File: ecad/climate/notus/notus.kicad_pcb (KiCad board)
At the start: 2 copper layers, 115 x 23 mm, 7 parts, among them J1 640454-2

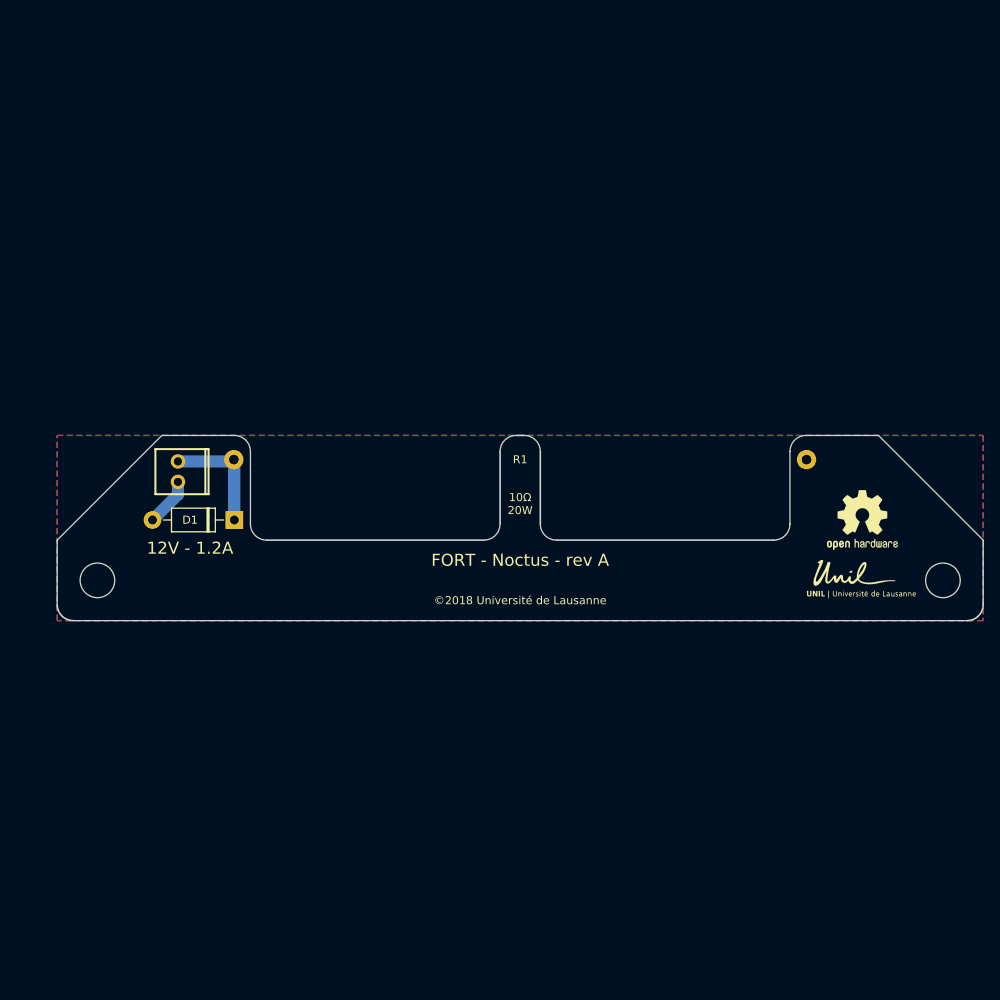
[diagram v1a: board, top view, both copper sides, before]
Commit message: Updates ecad for assembly production
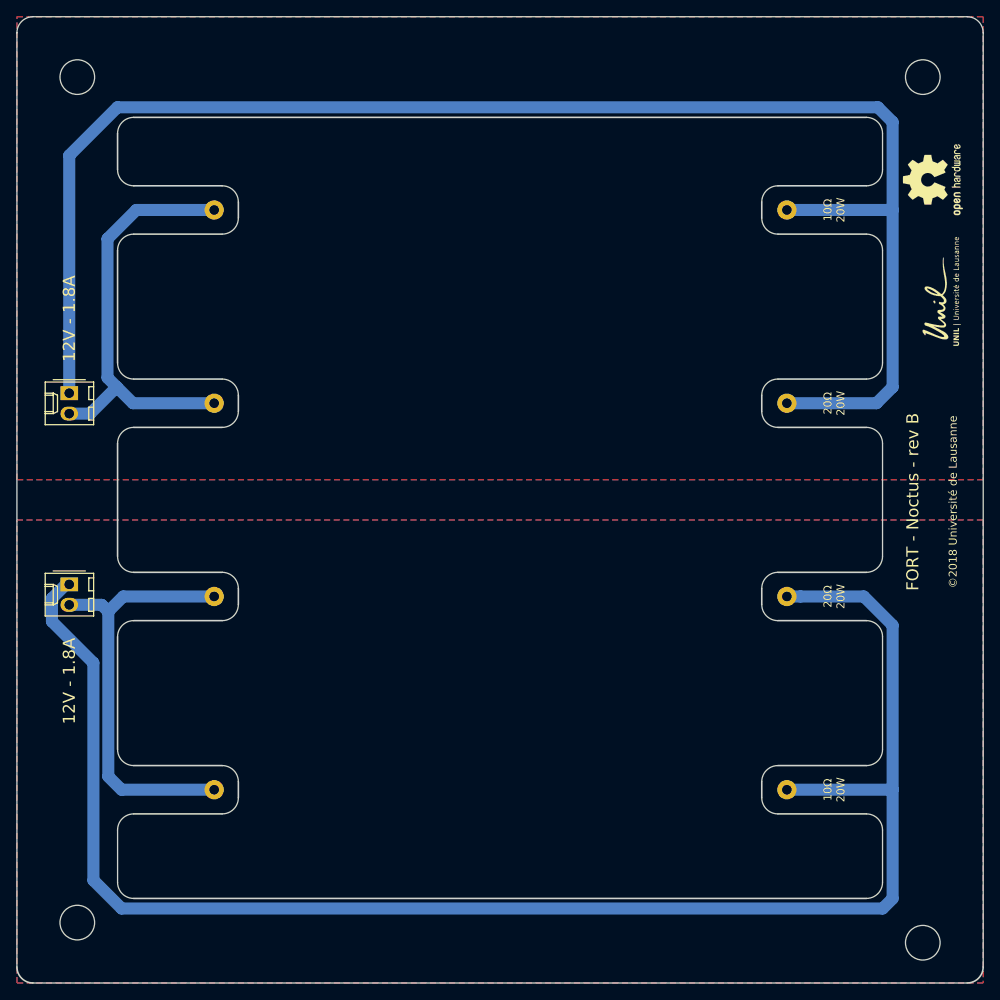
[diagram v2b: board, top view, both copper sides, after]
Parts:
- removed D1: 1N4001, Diode_THT:D_DO-41_SOD81_P10.16mm_Horizontal
- added J2: 6410-02A, Connector_Molex:Molex_KK-254_AE-6410-02A_1x02_P2.54mm_Vertical, F.Cu at (96.5, 76.8)
- added MH3: MountingHole, MountingHole:MountingHole_4.3mm_M4_DIN965, F.Cu at (202.5, 37.5)
- added MH4: MountingHole, MountingHole:MountingHole_4.3mm_M4_DIN965, F.Cu at (97.5, 37.5)
- added R2: 20R, 20W, Resistor_THT:R_Axial_Power_L60.0mm_W14.0mm_P71.12mm, F.Cu at (114.5, 102.0)
- added R3: 20R, 20W, Resistor_THT:R_Axial_Power_L60.0mm_W14.0mm_P71.12mm, F.Cu at (114.5, 54.0)
- added R4: 10R, 20W, Resistor_THT:R_Axial_Power_L60.0mm_W14.0mm_P71.12mm, F.Cu at (114.5, 78.0)
- J1: value 640454-2 -> 6410-02A; footprint FORT:640454-2 -> Connector_Molex:Molex_KK-254_AE-6410-02A_1x02_P2.54mm_Vertical
- moved R1 55.9 mm to (114.5, 126.0), turned to 0 degrees
- moved MH2 45.1 mm to (202.5, 145.0)
- moved REF** 43.1 mm to (203.8, 50.2), turned to 90 degrees
- moved MH1 42.6 mm to (97.5, 142.5)
- moved G*** 37.4 mm to (205.0, 64.0), turned to 90 degrees
- moved J1 19.4 mm to (96.5, 100.5)
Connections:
- net /PWM_+ renamed /PWM_A
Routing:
- net /PWM_B: track 0.00 -> 195.0 mm
- net /PWM_A: track 14.6 -> 202.9 mm
- net GNDA: track 0.00 -> 53.8 mm
- net GND: track 6.04 -> 53.4 mm
- added copper zone on B.Cu, net GNDA
- added copper zone on F.Cu, net GNDA
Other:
- board size 115 x 23 mm -> 120 x 120 mm
- board text added: "12V - 1.8A"
- board text added: "20Ω 20W"
- board text added: "FORT - Noctus - rev B"
- board text removed: "12V - 1.2A"
- board text removed: "FORT - Noctus - rev A"

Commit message: Updates kicad data.
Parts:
- moved MH2 2.50 mm to (202.5, 142.5)
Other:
- board text added: "FORT - Noctus - rev C"
- board text removed: "FORT - Noctus - rev B"
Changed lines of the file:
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@@
-(kicad_pcb (version 20171130) (host pcbnew 5.0.0+dfsg1-2~bpo9+1)
+(kicad_pcb (version 20171130) (host pcbnew 5.0.2+dfsg1-1~bpo9+1)
   (general
     (thickness 1.6)
@@
     (pad_drill 4.3)
     (pad_to_mask_clearance 0.2)
+    (solder_mask_min_width 0.25)
     (aux_axis_origin 0 0)
     (visible_elements FFFFFF7F)
@@
   )
   (module MountingHole:MountingHole_4.3mm_M4_DIN965 (layer F.Cu)
-    (at 202.5 145)
+    (at 202.5 142.5)
     (descr "Mounting Hole 4.3mm, no annular, M4, DIN965")
     (tags "mounting hole 4.3mm no annular m4 din965")
@@
     (effects (font (size 1 1) (thickness 0.25)))
   )
-  (gr_text "FORT - Noctus - rev B" (at 201.25 90.25 90) (layer F.SilkS)
+  (gr_text "FORT - Noctus - rev C" (at 201.25 90.25 90) (layer F.SilkS)
     (effects (font (size 1.5 1.5) (thickness 0.3)))
   )

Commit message: Starts a brand new notus
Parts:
- removed G***: LOGO, FORT:UNIL-LOGO_13.8x5.1mm
- removed MH1, MH2, MH3, MH4: MountingHole, MountingHole:MountingHole_4.3mm_M4_DIN965
- removed R1, R4: 10R, 20W, Resistor_THT:R_Axial_Power_L60.0mm_W14.0mm_P71.12mm
- removed R2, R3: 20R, 20W, Resistor_THT:R_Axial_Power_L60.0mm_W14.0mm_P71.12mm
- removed REF**: OSHW-Logo2_9.8x8mm_SilkScreen, Symbol:OSHW-Logo2_9.8x8mm_SilkScreen
- added U1: CPC1966YX6, FORT:SIP4_LittleFuse_CPC19X6yX6, F.Cu at (178.1, 50.0)
- added U2: CPC1966YX6, FORT:SIP4_LittleFuse_CPC19X6yX6, F.Cu at (183.2, 50.0)
- J1, J2: value 6410-02A -> Screw_Terminal_01x03; footprint Connector_Molex:Molex_KK-254_AE-6410-02A_1x02_P2.54mm_Vertical -> TerminalBlock:TerminalBlock_bornier-3_P5.08mm
- moved J2 77.3 mm to (173.0, 66.0), turned to 0 degrees
- moved J1 68.7 mm to (155.9, 66.0), turned to 0 degrees
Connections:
- J1 pad 1: /PWM_A -> /AC_L
- J1 pad 2: GND -> Earth
- J2 pad 1: /PWM_B -> /AC_N
- J2 pad 2: GNDA -> /AC_L1
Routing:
- net /PWM_A: track 202.9 -> 0.00 mm
- net /PWM_B: track 195.0 -> 0.00 mm
- net GNDA: track 53.8 -> 0.00 mm
- net GND: track 53.4 -> 0.00 mm
- net /AC_L: track 0.00 -> 36.3 mm
- net /AC_L2: track 0.00 -> 7.11 mm
- net /AC_L1: track 0.00 -> 7.11 mm
- net /AC_N: track 0.00 -> 6.92 mm
- removed copper zone on B.Cu, net GND
- removed copper zone on F.Cu, net GND
- removed copper zone on B.Cu, net GNDA
- removed copper zone on F.Cu, net GNDA
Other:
- board outline removed
- net class Default removed
- board text removed: "10Ω 20W"
- board text removed: "12V - 1.8A"
- board text removed: "20Ω 20W"
- board text removed: "FORT - Noctus - rev C"
- board text removed: "©2018 Université de Lausanne"

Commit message: Layout Notus Rev C
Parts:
- added C1: 2.2u, Capacitor_SMD:C_1210_3225Metric, F.Cu at (113.2, 110.4)
- added C10: 100n, Capacitor_SMD:C_0402_1005Metric, F.Cu at (135.0, 103.4)
- added C11: 100n, Capacitor_SMD:C_0402_1005Metric, F.Cu at (150.1, 97.2)
- added C12: 2u2, Capacitor_SMD:C_0402_1005Metric, F.Cu at (146.8, 104.6)
- added C13: 100n, Capacitor_SMD:C_0402_1005Metric, F.Cu at (146.8, 102.6)
- added C14: 100n, Capacitor_SMD:C_0402_1005Metric, F.Cu at (143.1, 106.6)
- added C15: 100n, Capacitor_SMD:C_0402_1005Metric, F.Cu at (139.4, 106.6)
- added C16: 100n, Capacitor_SMD:C_0402_1005Metric, F.Cu at (135.0, 102.5)
- added C17: 100n, Capacitor_SMD:C_0402_1005Metric, F.Cu at (139.5, 97.4)
- added C18: 100n, Capacitor_SMD:C_0402_1005Metric, F.Cu at (144.2, 97.4)
- added C19: 100n, Capacitor_SMD:C_0402_1005Metric, F.Cu at (137.4, 96.9)
- added C2: 100n, Capacitor_SMD:C_0603_1608Metric, F.Cu at (114.0, 108.0)
- added C3: 1u, Capacitor_SMD:C_0603_1608Metric, F.Cu at (119.1, 105.4)
- added C4: 100n, Capacitor_SMD:C_0402_1005Metric, F.Cu at (117.1, 106.5)
- added C5: 10u, Capacitor_SMD:C_0805_2012Metric, F.Cu at (120.2, 111.8)
- added C6: 15p, Capacitor_SMD:C_0402_1005Metric, F.Cu at (131.4, 98.7)
- added C7: 15p, Capacitor_SMD:C_0402_1005Metric, F.Cu at (131.4, 103.9)
- added C8: 2u2, Capacitor_SMD:C_0402_1005Metric, F.Cu at (146.8, 103.6)
- added C9: 100n, Capacitor_SMD:C_0402_1005Metric, F.Cu at (146.8, 101.6)
- added D1: ESD752DBZR, Package_TO_SOT_SMD:SOT-23, F.Cu at (105.2, 114.7)
- added F1: 3A, Fuse:Fuseholder_Clip-5x20mm_Bel_FC-203-22_Lateral_P17.80x5.00mm_D1.17mm_Horizontal, F.Cu at (139.3, 124.2)
- added J3: JST PH, Connector_JST:JST_PH_B4B-PH-SM4-TB_1x04-1MP_P2.00mm_Vertical, F.Cu at (107.2, 128.9)
- added J4: JST PH, Connector_JST:JST_PH_B4B-PH-SM4-TB_1x04-1MP_P2.00mm_Vertical, F.Cu at (107.2, 120.4)
- added J5: JST SH, Connector_JST:JST_SH_BM03B-SRSS-TB_1x03-1MP_P1.00mm_Vertical, F.Cu at (142.0, 94.3)
- added L1: 47u, Inductor_SMD:L_Taiyo-Yuden_NR-40xx, F.Cu at (119.9, 108.5)
- added P1: IEC320 C14, FORT:AdamTech_IEC-A-4, F.Cu at (128.5, 135.5)
- added Q1: RE1C002UN, Package_TO_SOT_SMD:SOT-416, F.Cu at (145.7, 108.9)
- added Q2: RE1C002UN, Package_TO_SOT_SMD:SOT-416, F.Cu at (145.7, 111.2)
- added R1: 220, Resistor_SMD:R_0402_1005Metric, F.Cu at (147.4, 108.7)
- added R2: 220, Resistor_SMD:R_0402_1005Metric, F.Cu at (147.4, 111.0)
- added R3: 7.5k, Resistor_SMD:R_0402_1005Metric, F.Cu at (111.6, 105.8)
- added R4: 10k, Resistor_SMD:R_0402_1005Metric, F.Cu at (111.6, 104.8)
- added R5: 1k, Resistor_SMD:R_0402_1005Metric, F.Cu at (133.6, 102.3)
- added REF**: MountingHole_2.7mm_M2.5, MountingHole:MountingHole_2.7mm_M2.5, F.Cu at (103.0, 137.0)
- added REF**: MountingHole_2.7mm_M2.5, MountingHole:MountingHole_2.7mm_M2.5, F.Cu at (155.0, 93.0)
- added REF**: MountingHole_3.2mm_M3, MountingHole:MountingHole_3.2mm_M3, F.Cu at (128.5, 111.5)
- added U3: LMR36500P3RPE, FORT:Texas_VQFN-HR-9_2.1x2.1mm_P0.5mm, F.Cu at (115.1, 105.7)
- added U4: W25Q16JVUXIQ, FORT:Winbond_USON-8-1EP_UX_2x3mm_P0.5mm_EP0.2x1.5mm, F.Cu at (148.1, 99.1)
- added U5: RP2040, Package_DFN_QFN:QFN-56-1EP_7x7mm_P0.4mm_EP3.2x3.2mm, F.Cu at (141.0, 102.0)
- added U6: TCAN3414, Package_TO_SOT_SMD:SOT-23-8, F.Cu at (134.8, 96.9)
- added Y1: ABM8-272-T3, Crystal:Crystal_SMD_3225-4Pin_3.2x2.5mm, F.Cu at (131.4, 101.3)
- J1: value Screw_Terminal_01x03 -> JST SH; footprint TerminalBlock:TerminalBlock_bornier-3_P5.08mm -> Connector_JST:JST_SH_BM03B-SRSS-TB_1x03-1MP_P1.00mm_Vertical
- J2: value Screw_Terminal_01x03 -> Terminal P5.08
- moved U1 73.6 mm to (149.9, 118.0)
- moved U2 73.6 mm to (155.0, 118.0)
- moved J2 72.6 mm to (144.8, 132.9)
- moved J1 47.2 mm to (138.0, 109.7)
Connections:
- net /AC_L1 renamed /AC_L_HEATER
- net /AC_L2 renamed /AC_L_FAN
- J1 pad 1: /AC_L -> /SWCLK
- J1 pad 2: Earth -> GND
- J1 pad 3: /AC_N -> /SWDIO
- U1 pad 1: unconnected-(U1-Pad1) -> Net-(R1-Pad1)
- U1 pad 2: unconnected-(U1-Pad2) -> +3V3
- U2 pad 1: unconnected-(U2-Pad1) -> Net-(R2-Pad1)
- U2 pad 2: unconnected-(U2-Pad2) -> +3V3
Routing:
- net +3V3: track 0.00 -> 105.8 mm
- net /CAN-: track 0.00 -> 57.7 mm
- net /CAN+: track 0.00 -> 57.1 mm
- net GND: track 0.00 -> 56.5 mm, vias 0 -> 51
- net /RUN: track 0.00 -> 50.2 mm
- net +12V: track 0.00 -> 22.6 mm
- net /AC_L_NP: track 0.00 -> 16.3 mm
- net /AC_L: track 36.3 -> 20.7 mm
- net /RG_VCC: track 0.00 -> 15.5 mm, vias 0 -> 2
- net +1V1: track 0.00 -> 15.1 mm, vias 0 -> 4
- net /SWDIO: track 0.00 -> 9.61 mm
- net /SWCLK: track 0.00 -> 9.54 mm
- net /XIN: track 0.00 -> 9.19 mm
- net /QSPI_IO3: track 0.00 -> 9.16 mm
- net Net-(R2-Pad1): track 0.00 -> 8.62 mm
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- added copper zone on F.Cu, net +12V
- added copper zone on F.Cu, net +1V1
- added copper zone on F.Cu, net +3V3
- added copper zone on F.Cu, net /RG_SW
- added copper zone on B.Cu, net GND
- added copper zone on F.Cu, net GND
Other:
- board outline added: 58 x 50 mm
- rule pad_to_mask_clearance: 0.2 -> 0
- board text added: "COLD"
- board text added: "HOT"

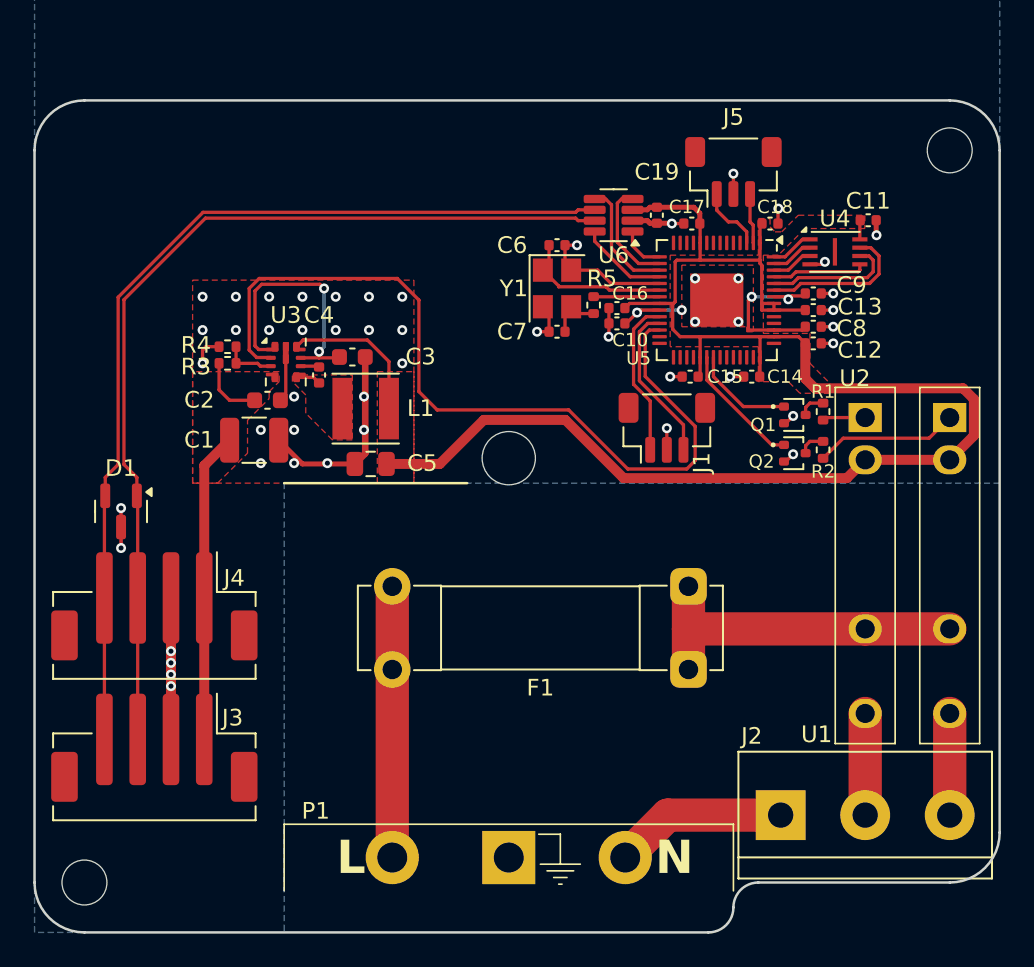
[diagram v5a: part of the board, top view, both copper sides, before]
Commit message: Finishes Notus MkII Rev A PCB
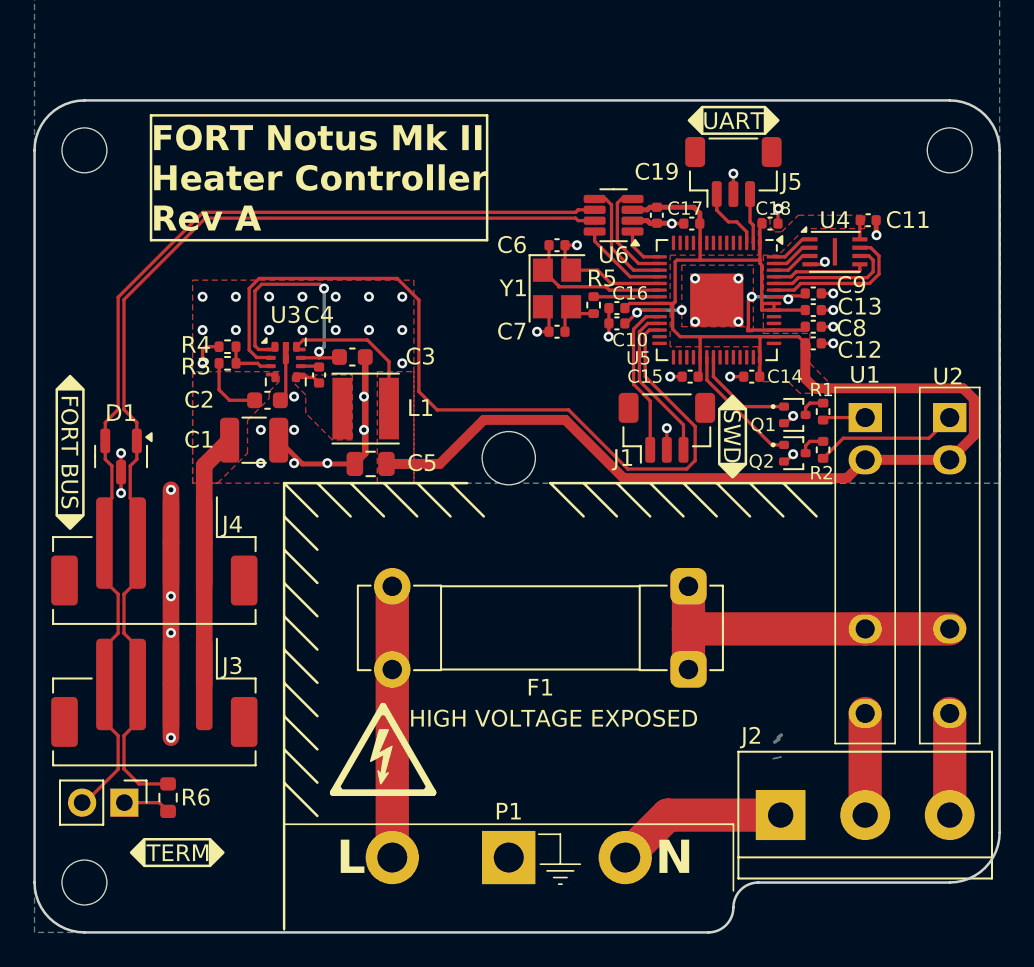
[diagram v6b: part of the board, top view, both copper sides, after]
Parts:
- added JP1: Term, Connector_PinHeader_2.54mm:PinHeader_1x02_P2.54mm_Vertical, F.Cu at (105.4, 132.2)
- added R6: 120, Resistor_SMD:R_0603_1608Metric, F.Cu at (108.0, 131.9)
- added REF**: Symbol_HighVoltage_Triangle_6x6mm_Copper, Symbol:Symbol_HighVoltage_Triangle_6x6mm_Copper, F.Cu at (121.0, 129.0)
- added REF**: MountingHole_2.7mm_M2.5, MountingHole:MountingHole_2.7mm_M2.5, F.Cu at (103.0, 93.0)
- added REF**: Symbol_HighVoltage_Triangle_6x6mm_Copper, Symbol:Symbol_HighVoltage_Triangle_6x6mm_Copper, B.Cu at (144.6, 128.1)
- added REF**: OSHW-Logo_7.5x8mm_SilkScreen, Symbol:OSHW-Logo_7.5x8mm_SilkScreen, B.Cu at (147.4, 99.6)
- J3, J4: footprint Connector_JST:JST_PH_B4B-PH-SM4-TB_1x04-1MP_P2.00mm_Vertical -> FORT:JST_PH_B4B-PH-SM4-TB_1x04-1MP_P2.00mm_Vertical
- moved J3 3.30 mm to (107.2, 125.6)
- moved J4 3.30 mm to (107.2, 117.1)
- moved D1 3.30 mm to (105.2, 111.4)
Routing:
- net GND: track 56.5 -> 62.9 mm
- net /CAN+: track 57.1 -> 63.3 mm
- net /CAN-: track 57.7 -> 63.9 mm
- net +12V: track 22.6 -> 19.3 mm
- net Net-(JP1-A): track 0.00 -> 2.84 mm
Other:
- board text added: "FORT BUS"
- board text added: "FORT Notus Mk II Heater Controller Rev A"
- board text added: "HIGH VOLTAGE EXPOSED"
- board text added: "SWD"
- board text added: "TERM"
- board text added: "UART"
- board text added: "© 2024 Université de Genève"

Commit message: Prepare Notus for prototyping
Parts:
- removed the REF** at (121.0, 129.0)
- removed the REF** at (144.6, 128.1)
- added R7: 10k, Resistor_SMD:R_0402_1005Metric, F.Cu at (123.8, 105.7)
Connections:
- U3 pad 1: /RG_VCC -> GND
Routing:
- net /RG_VCC: track 15.5 -> 2.35 mm, vias 2 -> 0
- net +3V3: track 105.8 -> 109.1 mm
- net /RUN: track 50.2 -> 49.4 mm

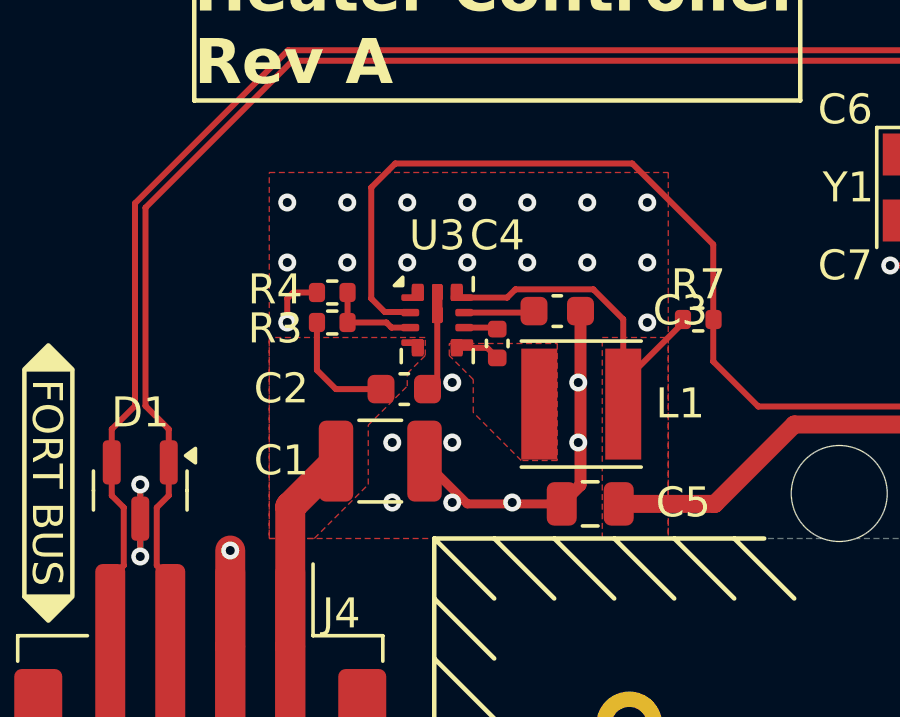
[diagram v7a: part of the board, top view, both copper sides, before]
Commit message: Updates Notus' MPN
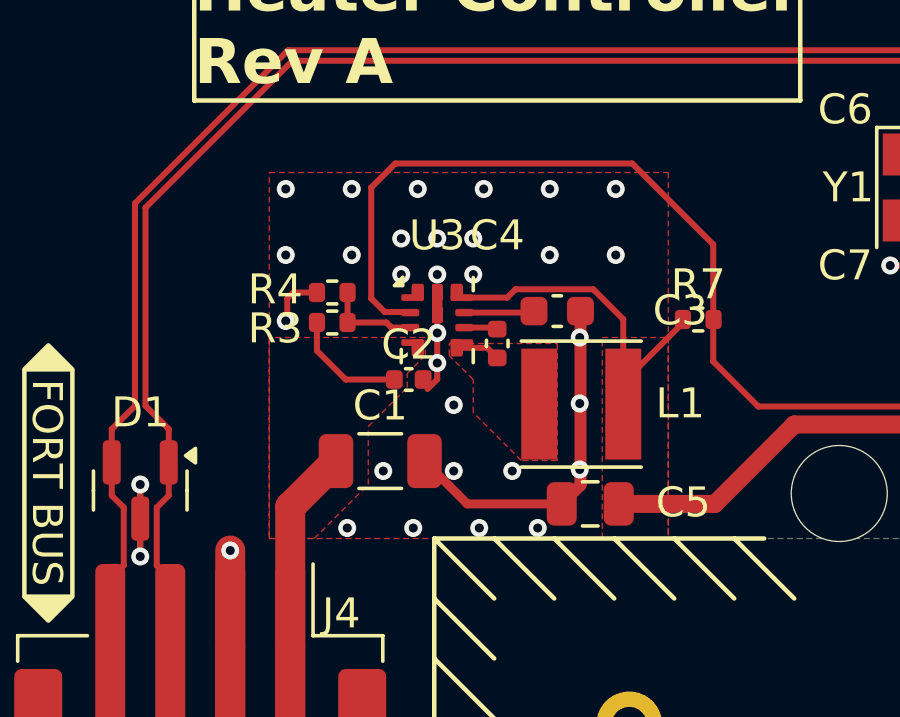
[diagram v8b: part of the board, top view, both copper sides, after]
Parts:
- C1: footprint Capacitor_SMD:C_1210_3225Metric -> Capacitor_SMD:C_1206_3216Metric
- C2: footprint Capacitor_SMD:C_0603_1608Metric -> Capacitor_SMD:C_0402_1005Metric
- D1: value ESD752DBZR -> CDSOT23-T24CAN
- L1: value 47u -> 47u
- U3: value LMR36500P3RPE -> LMR36501P3RPE
- moved C2 0.35 mm to (114.2, 107.7)
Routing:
- net GND: vias 51 -> 57
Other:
- board text added: "WayWayWay"
